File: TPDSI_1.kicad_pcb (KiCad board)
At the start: 2 copper layers, 83.8 x 61 mm, 56 parts, among them J1 Conn_01x02_Male, J2 Conn_01x02_Male, J3 Conn_01x10_Male, J4 Conn_01x04_Male, J5 Conn_01x04_Male, J6 Conn_01x06_Male, J7 Conn_01x02_Male, Q1 Q_NPN_BCE, Q2 Q_NPN_BCE, SW1 SW_Push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

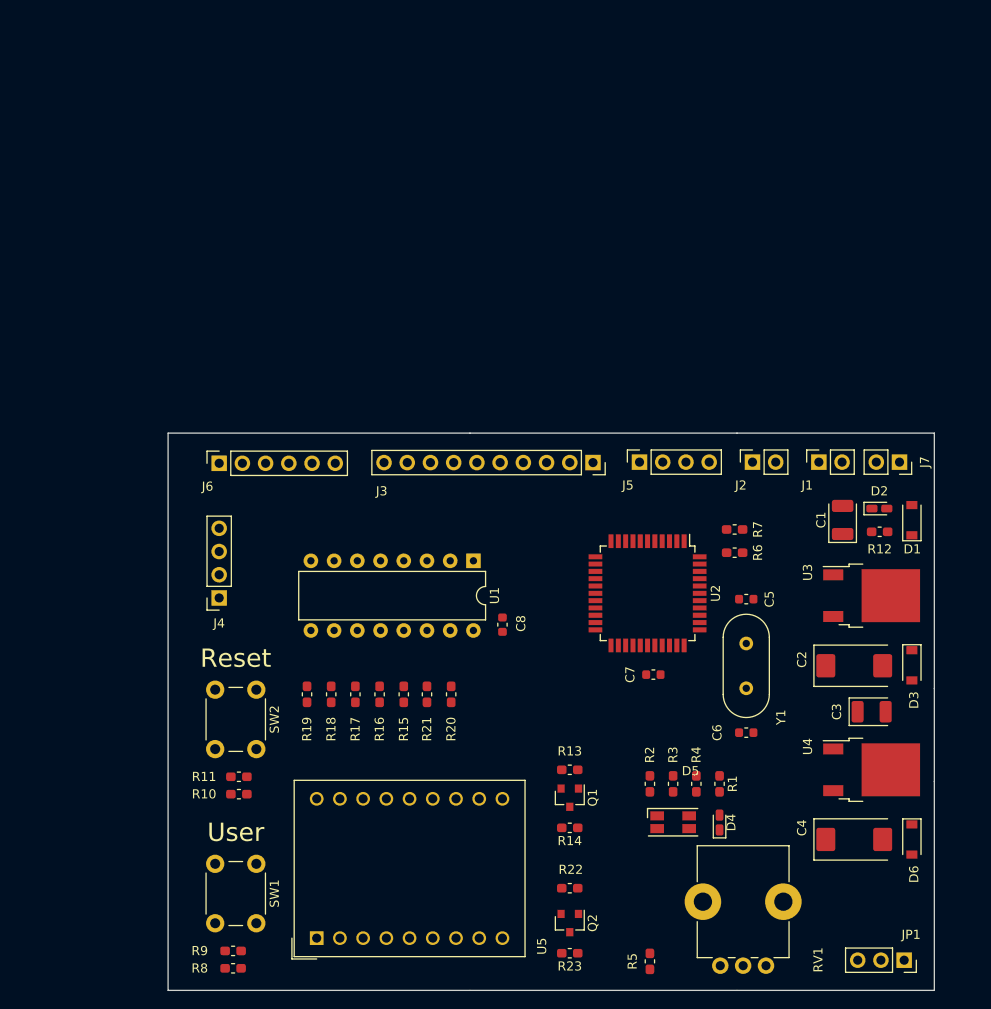
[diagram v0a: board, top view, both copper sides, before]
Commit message: Se reorganiza componenentes lineas mas limpias y analógicas mas cerca,Se cambia potenciometro y bornera de alimentación, se colocan perforaciones en la tarjeta
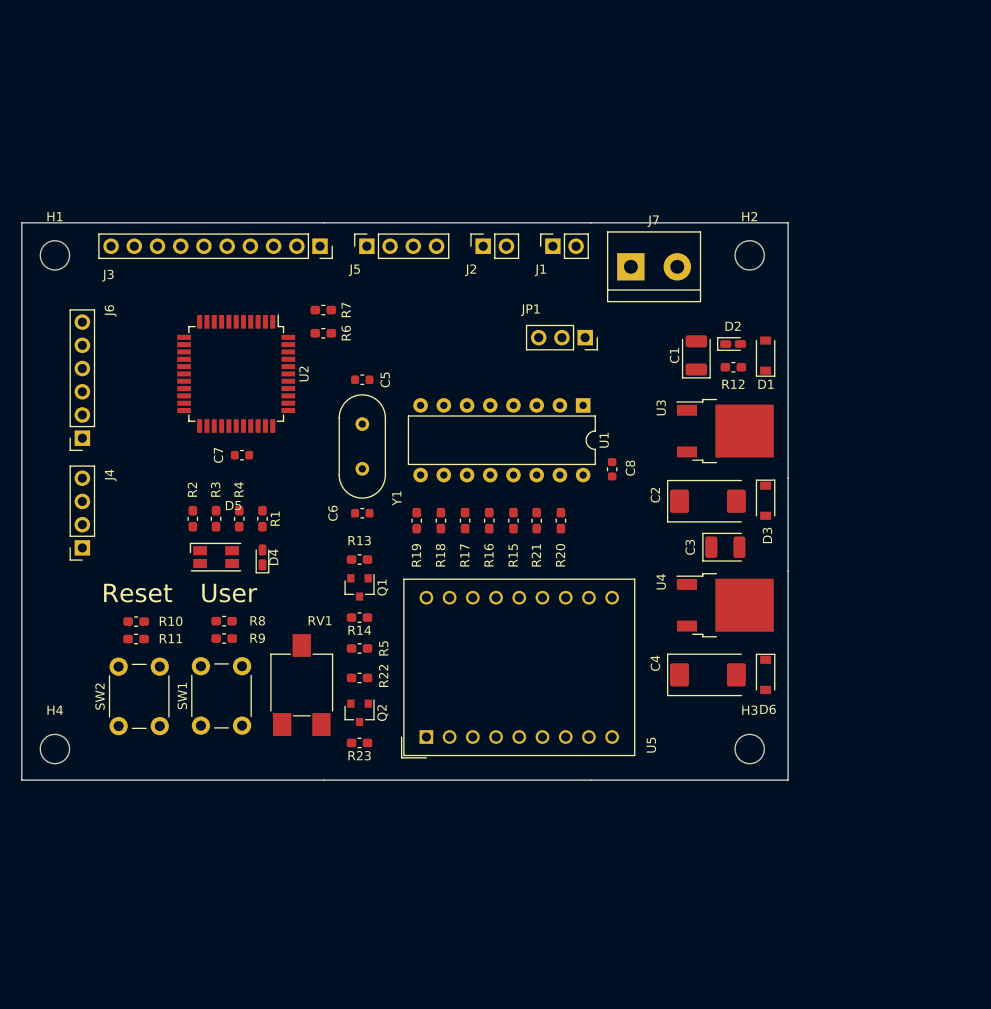
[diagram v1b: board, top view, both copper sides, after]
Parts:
- added H1: MountingHole, MountingHole:MountingHole_3.2mm_M3, F.Cu at (91.0, 88.0)
- added H2: MountingHole, MountingHole:MountingHole_3.2mm_M3, F.Cu at (167.0, 88.0)
- added H3: MountingHole, MountingHole:MountingHole_3.2mm_M3, F.Cu at (167.0, 142.0)
- added H4: MountingHole, MountingHole:MountingHole_3.2mm_M3, F.Cu at (91.0, 142.0)
- J7: value Conn_01x02_Male -> Screw_Terminal_01x02; footprint Connector_PinSocket_2.54mm:PinSocket_1x02_P2.54mm_Vertical -> TerminalBlock:TerminalBlock_bornier-2_P5.08mm
- RV1: footprint Potentiometer_THT:Potentiometer_Alps_RK09K_Single_Vertical -> Potentiometer_SMD:Potentiometer_ACP_CA6-VSMD_Vertical
- moved JP1 76.5 mm to (149.0, 97.0)
- moved RV1 59.3 mm to (118.0, 135.0)
- moved R4 57.8 mm to (111.2, 116.8)
- moved D4 57.8 mm to (113.7, 121.0)
- moved R1 57.8 mm to (113.7, 116.8)
- moved R2 57.8 mm to (106.1, 116.8)
- moved D5 57.8 mm to (108.6, 121.0)
- moved R3 57.8 mm to (108.6, 116.8)
- moved R6 51.0 mm to (120.4, 96.5)
- moved R7 51.0 mm to (120.4, 94.0)
- moved U2 51.0 mm to (110.8, 101.0)
- moved C7 51.0 mm to (111.5, 109.9)
- moved C5 48.4 mm to (124.6, 101.6)
- moved C6 48.4 mm to (124.6, 116.2)
- moved Y1 48.4 mm to (124.6, 111.4)
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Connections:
- J7 pad 1: /9V0 -> GND
- J7 pad 2: GND -> /9V0

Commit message: Se agrega recomendaciones  de jacobo salvador
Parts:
- moved JP1 5.00 mm to (154.0, 97.0), turned to 0 degrees
- moved R6 2.24 mm to (122.4, 95.5)
- moved R7 2.24 mm to (122.4, 93.0)
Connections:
- net /sheet5D0426A9/MCLR_VPP renamed /Microcontroller/MCLR_VPP
- net /sheet5D0426A9/PGM(LVP) renamed /Microcontroller/PGM(LVP)
- net /sheet5D0426A9/RD0 renamed /Microcontroller/RD0
- net /sheet5D0426A9/RD1 renamed /Microcontroller/RD1
- net /sheet5D0426A9/RD2 renamed /Microcontroller/RD2
- net /sheet5D0426A9/RD3 renamed /Microcontroller/RD3
- net /sheet5D0426A9/RX renamed /Microcontroller/RX
- net /sheet5D0426A9/TX renamed /Microcontroller/TX
- net /sheet5D0426A9/USER_BUTTON renamed /Microcontroller/USER_BUTTON
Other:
- board text added: "JBN-DCI CESE-2019"

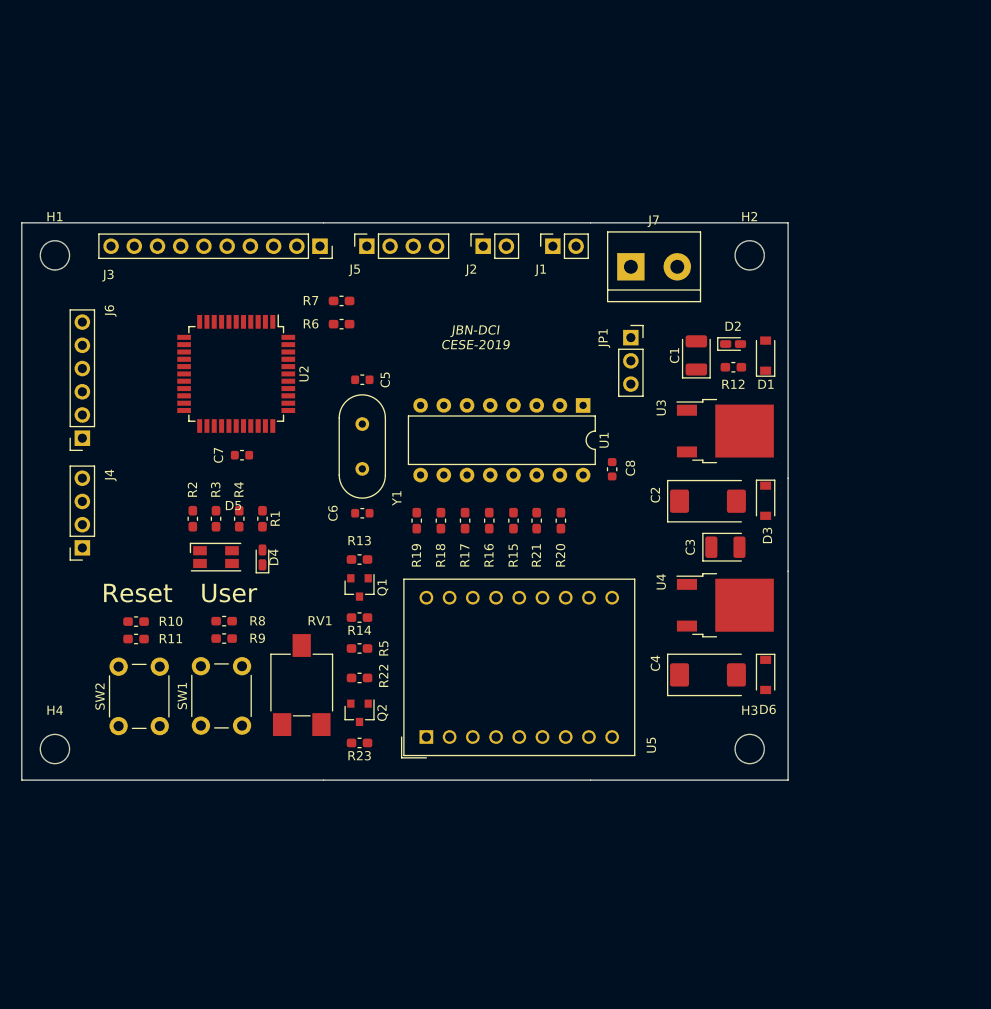
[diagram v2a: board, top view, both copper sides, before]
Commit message: Se agrega info del circuito,prolijidad en conexiones  se corrije,ERC Warninsg no errores,pendinete Datasheet y algunos numeros de parte,Comentario esquematico1: no es necesario con los labels que esta considero que esta ok, componentes los dejo en 0603, grilla en pcb 0.127 mm a criterio propio, se colocan fiduciales, pendiente lo demas de PCB.
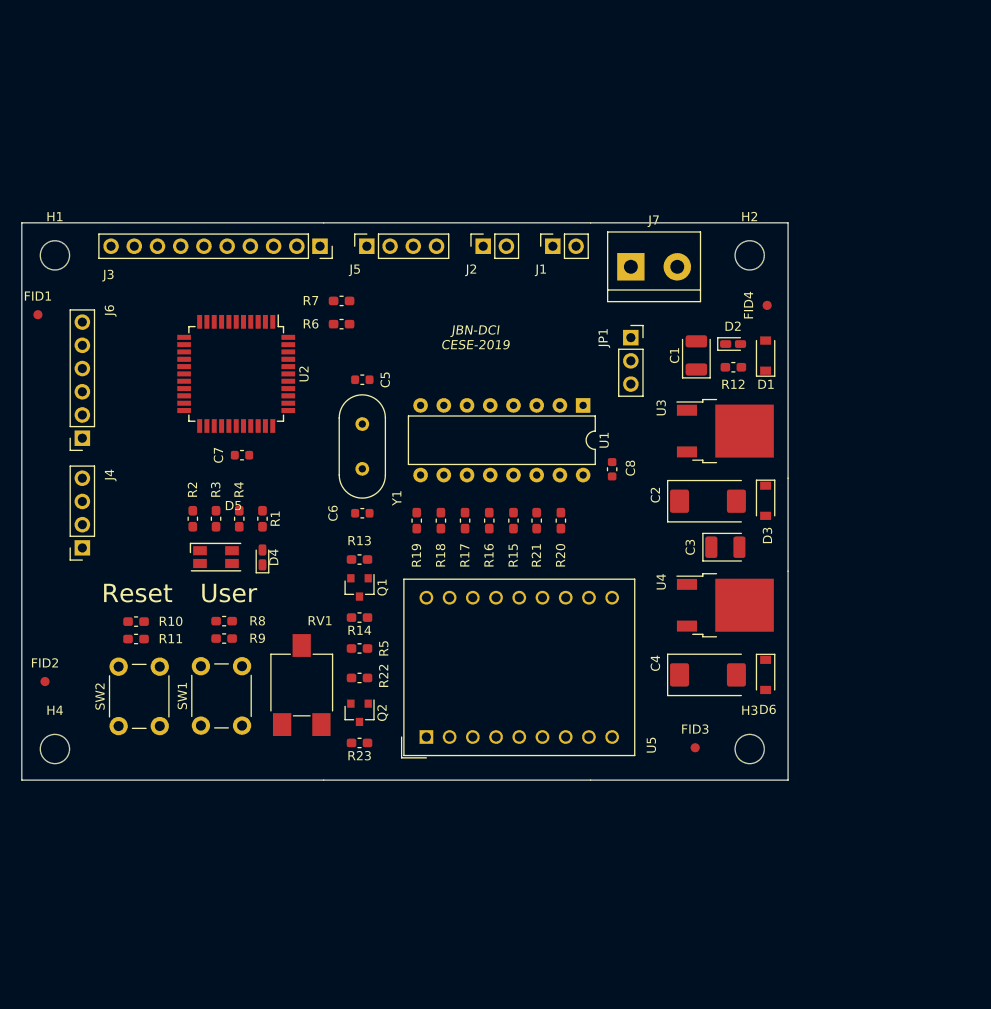
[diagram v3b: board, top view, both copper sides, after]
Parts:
- added FID1: Fiducial, Fiducial:Fiducial_1mm_Mask2mm, F.Cu at (89.1, 94.5)
- added FID2: Fiducial, Fiducial:Fiducial_1mm_Mask2mm, F.Cu at (89.9, 134.6)
- added FID3: Fiducial, Fiducial:Fiducial_1mm_Mask2mm, F.Cu at (161.0, 141.9)
- added FID4: Fiducial, Fiducial:Fiducial_1mm_Mask2mm, F.Cu at (168.9, 93.5)
- D1: value D -> 1n4148
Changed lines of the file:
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@@
     (tracks 0)
     (zones 0)
-    (modules 60)
+    (modules 64)
     (nets 76)
   )
@@
     (add_net VDD)
   )
+  (module Fiducial:Fiducial_1mm_Mask2mm (layer F.Cu)
+    (at 168.91 93.472 90)
+    (descr "Circular Fiducial, 1mm bare copper, 2mm soldermask opening (Level A)")
+    (tags fiducial)
+    (attr smd)
+    (fp_text reference FID4 (at 0 -2 90) (layer F.SilkS)
+      (effects (font (size 1 1) (thickness 0.15)))
+    )
+    (fp_text value Fiducial (at 0 2 90) (layer F.Fab)
+      (effects (font (size 1 1) (thickness 0.15)))
+    )
+    (fp_circle (center 0 0) (end 1.25 0) (layer F.CrtYd) (width 0.05))
+    (fp_text user %R (at 0 0 90) (layer F.Fab)
+      (effects (font (size 0.4 0.4) (thickness 0.06)))
+    )
+    (fp_circle (center 0 0) (end 1 0) (layer F.Fab) (width 0.1))
+    (pad "" smd circle (at 0 0 90) (size 1 1) (layers F.Cu F.Mask)
+      (solder_mask_margin 0.5) (clearance 0.5))
+  )
+  (module Fiducial:Fiducial_1mm_Mask2mm (layer F.Cu)
+    (at 161.036 141.859)
+    (descr "Circular Fiducial, 1mm bare copper, 2mm soldermask opening (Level A)")
+    (tags fiducial)
+    (attr smd)
+    (fp_text reference FID3 (at 0 -2) (layer F.SilkS)
+      (effects (font (size 1 1) (thickness 0.15)))
+    )
+    (fp_text value Fiducial (at 0 2) (layer F.Fab)
+      (effects (font (size 1 1) (thickness 0.15)))
+    )
+    (fp_circle (center 0 0) (end 1.25 0) (layer F.CrtYd) (width 0.05))
+    (fp_text user %R (at 0 0) (layer F.Fab)
+      (effects (font (size 0.4 0.4) (thickness 0.06)))
+    )
+    (fp_circle (center 0 0) (end 1 0) (layer F.Fab) (width 0.1))
+    (pad "" smd circle (at 0 0) (size 1 1) (layers F.Cu F.Mask)
+      (solder_mask_margin 0.5) (clearance 0.5))
+  )
+  (module Fiducial:Fiducial_1mm_Mask2mm (layer F.Cu)
+    (at 89.916 134.62)
+    (descr "Circular Fiducial, 1mm bare copper, 2mm soldermask opening (Level A)")
+    (tags fiducial)
+    (attr smd)
+    (fp_text reference FID2 (at 0 -2) (layer F.SilkS)
+      (effects (font (size 1 1) (thickness 0.15)))
+    )
+    (fp_text value Fiducial (at 0 2) (layer F.Fab)
+      (effects (font (size 1 1) (thickness 0.15)))
+    )
+    (fp_circle (center 0 0) (end 1.25 0) (layer F.CrtYd) (width 0.05))
+    (fp_text user %R (at 0 0) (layer F.Fab)
+      (effects (font (size 0.4 0.4) (thickness 0.06)))
+    )
+    (fp_circle (center 0 0) (end 1 0) (layer F.Fab) (width 0.1))
+    (pad "" smd circle (at 0 0) (size 1 1) (layers F.Cu F.Mask)
+      (solder_mask_margin 0.5) (clearance 0.5))
+  )
+  (module Fiducial:Fiducial_1mm_Mask2mm (layer F.Cu)
+    (at 89.140999 94.488)
+    (descr "Circular Fiducial, 1mm bare copper, 2mm soldermask opening (Level A)")
+    (tags fiducial)
+    (attr smd)
+    (fp_text reference FID1 (at 0 -2) (layer F.SilkS)
+      (effects (font (size 1 1) (thickness 0.15)))
+    )
+    (fp_text value Fiducial (at 0 2) (layer F.Fab)
+      (effects (font (size 1 1) (thickness 0.15)))
+    )
+    (fp_circle (center 0 0) (end 1.25 0) (layer F.CrtYd) (width 0.05))
+    (fp_text user %R (at 0 0) (layer F.Fab)
+      (effects (font (size 0.4 0.4) (thickness 0.06)))
+    )
+    (fp_circle (center 0 0) (end 1 0) (layer F.Fab) (width 0.1))
+    (pad "" smd circle (at 0 0) (size 1 1) (layers F.Cu F.Mask)
+      (solder_mask_margin 0.5) (clearance 0.5))
+  )
   (module MountingHole:MountingHole_3.2mm_M3 (layer F.Cu)
     (at 91 142)
@@
       (effects (font (size 1 1) (thickness 0.15)))
     )
-    (fp_text value D (at 0 2.1 90) (layer F.Fab)
-      (effects (font (size 1 1) (thickness 0.15)))
-    )
+    (fp_text value 1n4148 (at 0 2.1 90) (layer F.Fab)
+      (effects (font (size 1 1) (thickness 0.15)))
+    )

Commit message: Se agrega reglas de pcb , se corrige ERC en sch, se agrega grilla 0.127(5 mils) , se agrega plano de tierra, keep out para perforaciones, se agrega rotulo , se rutea pocas pistas
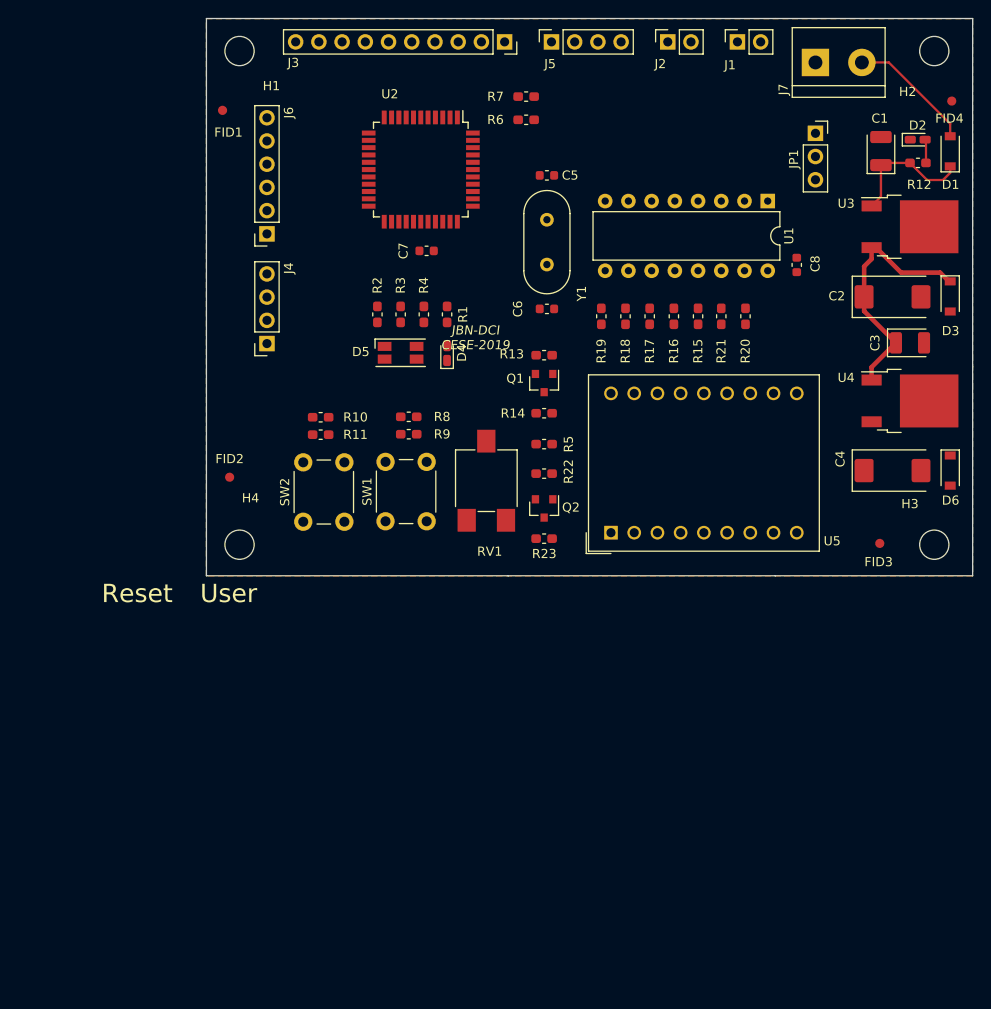
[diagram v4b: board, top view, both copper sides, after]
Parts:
- moved U5 30.1 mm to (151.8, 118.3)
- moved SW2 30.1 mm to (118.2, 117.1)
- moved C1 30.1 mm to (181.4, 76.6)
- moved C6 30.1 mm to (144.8, 93.9)
- moved C7 30.1 mm to (131.7, 87.5)
- moved FID1 30.1 mm to (109.3, 72.1)
- moved FID3 30.1 mm to (181.2, 119.5)
- moved H2 30.1 mm to (187.2, 65.6)
- moved H3 30.1 mm to (187.2, 119.6)
- moved J1 30.1 mm to (165.7, 64.6)
- moved J2 30.1 mm to (158.0, 64.6)
- moved J3 30.1 mm to (140.2, 64.6)
- moved J7 30.1 mm to (174.2, 66.9)
- moved JP1 30.1 mm to (174.2, 74.6)
- moved Q2 30.1 mm to (144.5, 115.7)
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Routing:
- net +5V: track 0.00 -> 27.5 mm
- net Net-(C1-Pad1): track 0.00 -> 14.4 mm
- net /9V0: track 0.00 -> 13.8 mm
- net Net-(D2-Pad2): track 0.00 -> 2.58 mm
- added copper zone on F.Cu, net GND
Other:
- net class Default: clearance 0.4 -> 0.2; trace_width 0.8 -> 0.254; via_dia 1 -> 0.8; via_drill 0.6 -> 0.4
- rule trace_clearance: 0.4 -> 0.2
- rule trace_min: 0.2 -> 0.254
- rule via_min_drill: 0.3 -> 0.4
- rule via_min_size: 0.4 -> 0.8
- board text added: "*Capas 2 *Ancho de pista 0.254 mm *Clearence 0.254 mm keep out circular *Diametro via 0.8mm *Tdro via 0.4mm"
- board text added: "*Grilla 0.254 mm"

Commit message: Se agrega plano gnd y ruteo de fuente con plano en vdd
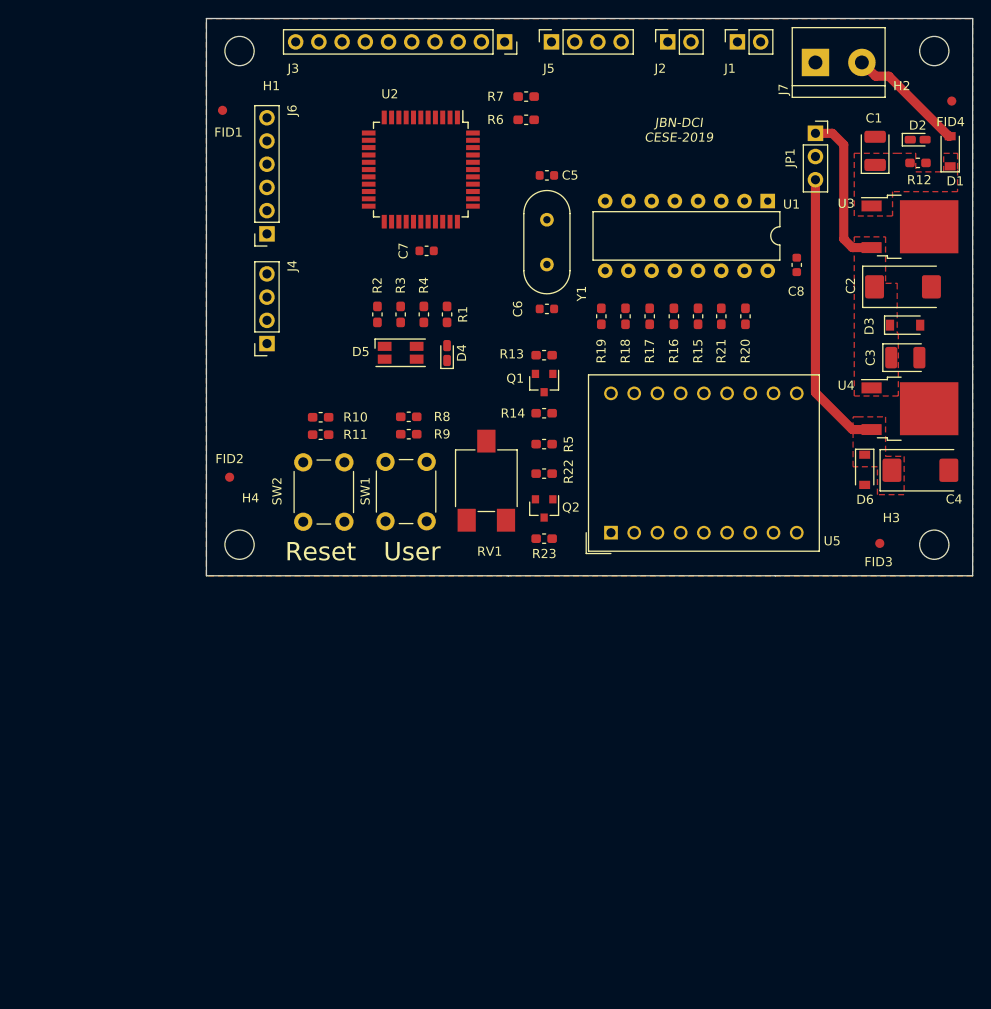
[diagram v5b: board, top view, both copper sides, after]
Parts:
- moved D6 9.36 mm to (179.6, 111.5)
- moved D3 5.85 mm to (184.0, 95.6), turned to 0 degrees
- moved C4 3.05 mm to (185.7, 111.5)
- moved C3 1.70 mm to (184.0, 99.2)
- moved C2 1.58 mm to (183.8, 91.4)
- moved U4 0.86 mm to (184.5, 104.8)
- moved C1 0.64 mm to (180.7, 76.6)
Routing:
- net +3V3: track 0.00 -> 31.1 mm
- net Net-(C1-Pad1): track 14.4 -> 0.00 mm
- net +5V: track 27.5 -> 17.4 mm
- net Net-(D2-Pad2): track 2.58 -> 0.00 mm
- net /9V0: track 13.8 -> 13.0 mm
- added copper zone on F.Cu, net +3V3
- added copper zone on F.Cu, net +5V
- added copper zone on F.Cu, net Net-(C1-Pad1)
